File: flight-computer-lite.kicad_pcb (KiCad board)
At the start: 2 copper layers, 65 x 65 mm, 19 parts, among them J1 USB_C_Receptacle_USB2.0_16P, J2 Micro_SD_Card_Det2, Q1 BSS138, U1 RP2040, U2 W25Q32JVZP, U3 ICM-42688-P, U4 BMI088, U5 LIS3MDL, U6 MS5611-01BA, U7 SHT4x, U8 SAM-M8Q

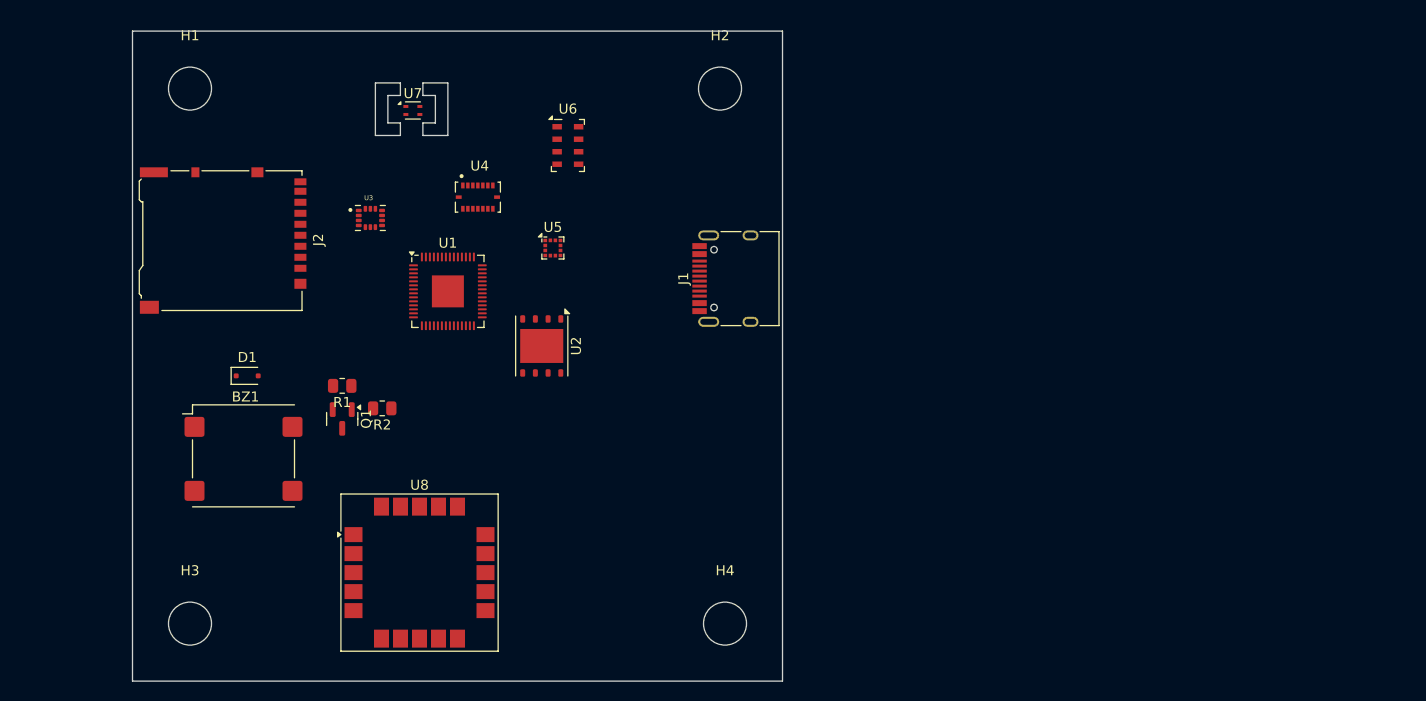
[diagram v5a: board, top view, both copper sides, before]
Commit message: Added battery, updated USB
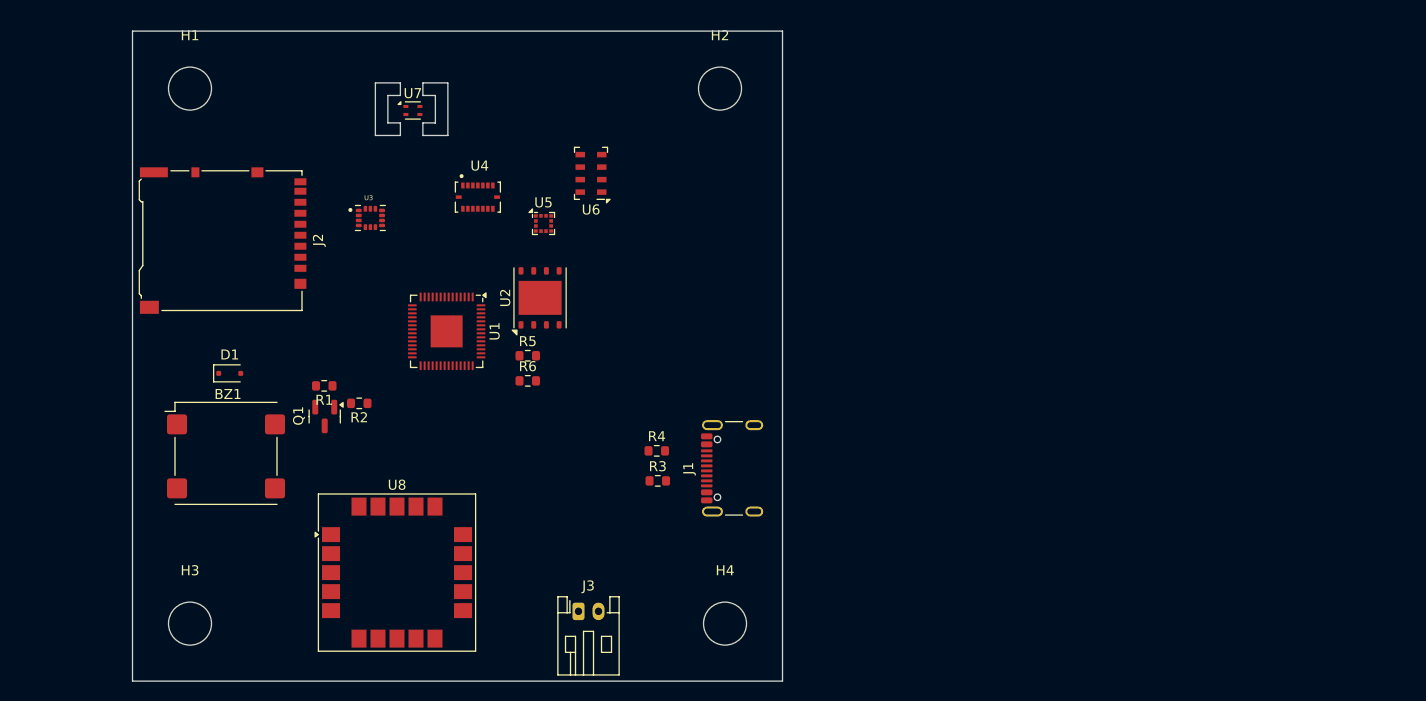
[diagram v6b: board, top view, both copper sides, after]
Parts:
- added J3: Conn_01x02_Pin, Connector_JST:JST_PH_S2B-PH-K_1x02_P2.00mm_Horizontal, F.Cu at (170.8, 113.3)
- added R3: 5.1K, Resistor_SMD:R_0603_1608Metric, F.Cu at (178.7, 100.2)
- added R4: 5.1K, Resistor_SMD:R_0603_1608Metric, F.Cu at (178.6, 97.2)
- added R5: 27.1, Resistor_SMD:R_0603_1608Metric, F.Cu at (165.7, 87.7)
- added R6: 27.1, Resistor_SMD:R_0603_1608Metric, F.Cu at (165.7, 90.2)
- J1: footprint Connector_USB:USB_C_Receptacle_HRO_TYPE-C-31-M-12 -> Connector_USB:USB_C_Receptacle_GCT_USB4105-xx-A_16P_TopMnt_Horizontal
- R1: footprint Resistor_SMD:R_0805_2012Metric -> Resistor_SMD:R_0603_1608Metric
- R2: value 100 -> 1K; footprint Resistor_SMD:R_0805_2012Metric -> Resistor_SMD:R_0603_1608Metric
- moved J1 19.0 mm to (187.2, 99.0)
- moved U2 4.82 mm to (166.9, 82.0), turned to 90 degrees
- moved U1 4.00 mm to (157.6, 85.3), turned to -90 degrees
- moved U6 3.62 mm to (172.0, 69.5), turned to 180 degrees
- moved U5 2.62 mm to (167.2, 74.5)
- moved R2 2.35 mm to (148.8, 92.5)
- moved U8 2.25 mm to (152.6, 109.4)
- moved R1 1.80 mm to (145.3, 90.8)
- moved BZ1 1.77 mm to (135.5, 97.5)
- moved D1 1.77 mm to (135.9, 89.5)
- moved Q1 1.77 mm to (145.4, 93.8)
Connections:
- net Net-(J1-VBUS-PadA4) renamed VBUS
- J1 pad A5: unconnected-(J1-CC1-PadA5) -> Net-(J1-CC1)
- J1 pad A6: unconnected-(J1-D+-PadA6) -> /CONN_USB_D+
- J1 pad A7: unconnected-(J1-D--PadA7) -> /CONN_USB_D-
- J1 pad B5: unconnected-(J1-CC2-PadB5) -> Net-(J1-CC2)
- J1 pad B6: unconnected-(J1-D+-PadB6) -> /CONN_USB_D+
- J1 pad B7: unconnected-(J1-D--PadB7) -> /CONN_USB_D-
- J1 pad S1: unconnected-(J1-SHIELD-PadS1) -> GND
- U1 pad 46: unconnected-(U1-USB_DM-Pad46) -> /CPU_USB_D-
- U1 pad 47: unconnected-(U1-USB_DP-Pad47) -> /CPU_USB_D+
- U7 pad 4: unconnected-(U7-VSS-Pad4) -> GND

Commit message: Added buttons, LEDs, TPs, and Miku
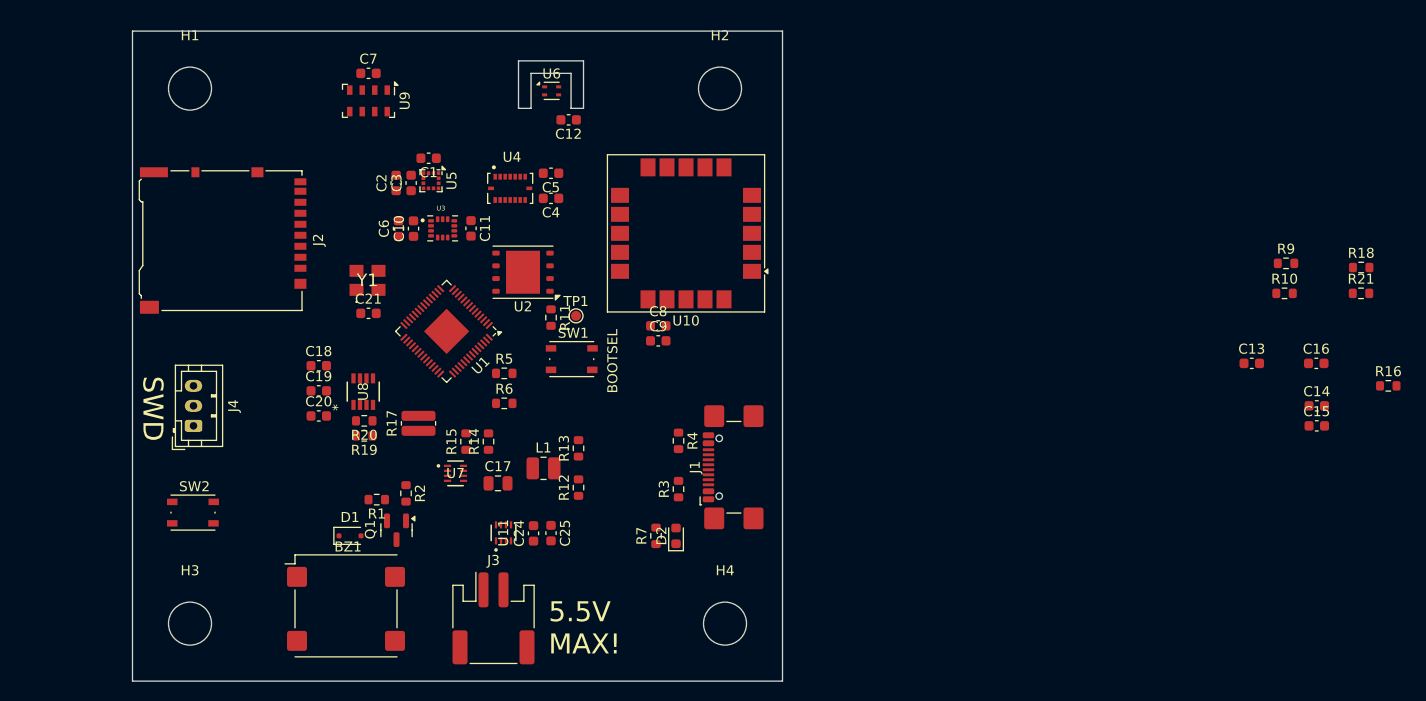
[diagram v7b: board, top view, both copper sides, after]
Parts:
- added C1: 0.1u, Capacitor_SMD:C_0603_1608Metric, F.Cu at (155.8, 68.0)
- added C10: 2.2u, Capacitor_SMD:C_0603_1608Metric, F.Cu at (154.2, 75.0)
- added C11: 10n, Capacitor_SMD:C_0603_1608Metric, F.Cu at (160.0, 75.0)
- added C12: 0.1u, Capacitor_SMD:C_0603_1608Metric, F.Cu at (169.8, 64.2)
- added C13: 0.1u, Capacitor_SMD:C_0603_1608Metric, F.Cu at (238.1, 88.5)
- added C14: 10u, Capacitor_SMD:C_0603_1608Metric, F.Cu at (244.6, 92.8)
- added C15: 0.1u, Capacitor_SMD:C_0603_1608Metric, F.Cu at (244.6, 94.8)
- added C16: 0.1u, Capacitor_SMD:C_0603_1608Metric, F.Cu at (244.5, 88.5)
- added C17: 47u, Capacitor_SMD:C_0805_2012Metric, F.Cu at (162.7, 100.5)
- added C18: 0.1u, Capacitor_SMD:C_0603_1608Metric, F.Cu at (144.8, 88.7)
- added C19: 2.2u, Capacitor_SMD:C_0603_1608Metric, F.Cu at (144.8, 91.2)
- added C2: 0.1u, Capacitor_SMD:C_0603_1608Metric, F.Cu at (152.5, 70.5)
- added C20: 0.1u, Capacitor_SMD:C_0603_1608Metric, F.Cu at (144.8, 93.8)
- added C21: 0.1u, Capacitor_SMD:C_0603_1608Metric, F.Cu at (149.8, 83.5)
- added C24: 2.2u, Capacitor_SMD:C_0603_1608Metric, F.Cu at (166.2, 105.5)
- added C25: 2.2u, Capacitor_SMD:C_0603_1608Metric, F.Cu at (168.0, 105.5)
- added C3: 1u, Capacitor_SMD:C_0603_1608Metric, F.Cu at (154.0, 70.5)
- added C4: 0.1u, Capacitor_SMD:C_0603_1608Metric, F.Cu at (168.0, 72.0)
- added C5: 0.1u, Capacitor_SMD:C_0603_1608Metric, F.Cu at (168.0, 69.5)
- added C6: 0.1u, Capacitor_SMD:C_0603_1608Metric, F.Cu at (152.8, 75.0)
- added C7: 0.1u, Capacitor_SMD:C_0603_1608Metric, F.Cu at (149.8, 59.5)
- added C8: 1u, Capacitor_SMD:C_0603_1608Metric, F.Cu at (178.7, 84.8)
- added C9: 0.1u, Capacitor_SMD:C_0603_1608Metric, F.Cu at (178.7, 86.2)
- added D2: LED, LED_SMD:LED_0603_1608Metric, F.Cu at (180.5, 105.8)
- added G***: LOGO, LRI_partlib:rocket_miku, B.Cu at (160.2, 85.2)
- added J4: Conn_01x03_Pin, Connector_JST:JST_PH_B3B-PH-K_1x03_P2.00mm_Vertical, F.Cu at (132.2, 94.8)
- added L1: 1u, Inductor_SMD:L_1008_2520Metric, F.Cu at (167.2, 99.0)
- added R10: I2C, Resistor_SMD:R_0603_1608Metric, F.Cu at (241.3, 81.5)
- added R11: 1k, Resistor_SMD:R_0603_1608Metric, F.Cu at (168.0, 83.9)
- added R12: 107k, Resistor_SMD:R_0603_1608Metric, F.Cu at (170.8, 100.9)
- added R13: 19.1k, Resistor_SMD:R_0603_1608Metric, F.Cu at (170.8, 97.0)
- added R14: 0R, Resistor_SMD:R_0603_1608Metric, F.Cu at (161.8, 96.3)
- added R15: 0R, Resistor_SMD:R_0603_1608Metric, F.Cu at (159.5, 96.3)
- added R16: 10k, Resistor_SMD:R_0603_1608Metric, F.Cu at (251.7, 90.8)
- added R17: 10m, Resistor_SMD:R_0612_1632Metric, F.Cu at (154.8, 94.5)
- added R18: I2C, Resistor_SMD:R_0603_1608Metric, F.Cu at (249.0, 78.9)
- added R19: 100, Resistor_SMD:R_0603_1608Metric, F.Cu at (149.3, 95.8)
- added R20: 100, Resistor_SMD:R_0603_1608Metric, F.Cu at (149.3, 94.2)
- added R21: I2C, Resistor_SMD:R_0603_1608Metric, F.Cu at (249.0, 81.5)
- added R7: R, Resistor_SMD:R_0603_1608Metric, F.Cu at (178.5, 105.8)
- added R9: I2C, Resistor_SMD:R_0603_1608Metric, F.Cu at (241.5, 78.5)
- added SW1: SW_Push, Button_Switch_SMD:SW_Push_1P1T_NO_Vertical_Wuerth_434133025816, F.Cu at (170.1, 88.1)
- added SW2: SW_Push, Button_Switch_SMD:SW_Push_1P1T_NO_Vertical_Wuerth_434133025816, F.Cu at (132.2, 103.4)
- added TP1: TestPoint, TestPoint:TestPoint_Pad_D1.0mm, F.Cu at (170.5, 83.8)
- added U10: SAM-M10Q, RF_GPS:ublox_SAM-M8Q, F.Cu at (181.5, 75.5)
- added U11: LM66200DRLR, LRI_partlib:LM66200, F.Cu at (163.3, 105.4)
- added U9: MS5611-01BA, Package_LGA:LGA-8_3x5mm_P1.25mm, F.Cu at (149.8, 62.2)
- added Y1: SiT1602BI-22-33E-12.000000E, LRI_partlib:SIT1602BI2233E12000000G, F.Cu at (149.7, 80.2)
- J1: footprint Connector_USB:USB_C_Receptacle_GCT_USB4105-xx-A_16P_TopMnt_Horizontal -> Connector_USB:USB_C_Receptacle_GCT_USB4110
- J3: footprint Connector_JST:JST_PH_S2B-PH-K_1x02_P2.00mm_Horizontal -> Connector_JST:JST_PH_S2B-PH-SM4-TB_1x02-1MP_P2.00mm_Horizontal
- U6: value MS5611-01BA -> SHT4x; footprint Package_LGA:LGA-8_3x5mm_P1.25mm -> Sensor_Humidity:Sensirion_DFN-4_1.5x1.5mm_P0.8mm_SHT4x_NoCentralPad
- U7: value SHT4x -> TPS631000DRLR; footprint Sensor_Humidity:Sensirion_DFN-4_1.5x1.5mm_P0.8mm_SHT4x_NoCentralPad -> LRI_partlib:TPS631000DRLR_TEX
- U8: value SAM-M8Q -> INA232AIDDFR; footprint RF_GPS:ublox_SAM-M8Q -> LRI_partlib:INA232AIDDFR
- moved U7 36.5 mm to (158.4, 99.5)
- moved D1 20.2 mm to (147.9, 105.8)
- moved BZ1 19.4 mm to (147.5, 112.8)
- moved U8 18.4 mm to (149.2, 91.3), turned to 90 degrees
- moved Q1 13.5 mm to (152.6, 105.2)
- moved R1 12.5 mm to (150.6, 102.1)
- moved U5 12.0 mm to (156.0, 70.2), turned to -90 degrees
- moved R2 10.1 mm to (153.5, 101.5), turned to -90 degrees
- moved U6 9.14 mm to (168.1, 61.2), turned to 0 degrees
- moved J3 8.53 mm to (162.2, 114.0)
- moved U3 7.30 mm to (157.2, 75.0)
- moved U4 3.34 mm to (163.9, 71.0)
- moved R6 3.25 mm to (163.3, 92.5)
- moved U2 3.08 mm to (165.2, 79.4), turned to 180 degrees
- moved R5 2.94 mm to (163.3, 89.5)
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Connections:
- net /CONN_USB_D+ renamed /USB_D+
- net /CONN_USB_D- renamed /USB_D-
- J1 pad S1: GND -> unconnected-(J1-SHIELD-PadS1)
- J2 pad 4: unconnected-(J2-VDD-Pad4) -> +3V3
- J2 pad 6: unconnected-(J2-VSS-Pad6) -> GND
- U1 pad 2: unconnected-(U1-GPIO0-Pad2) -> /I2C_1_SDA
- U1 pad 20: unconnected-(U1-XIN-Pad20) -> /XIN
- U1 pad 3: unconnected-(U1-GPIO1-Pad3) -> /I2C_1_SCL
- U1 pad 4: unconnected-(U1-GPIO2-Pad4) -> /I2C Bus 2/I2C_2_SDA
- U1 pad 5: unconnected-(U1-GPIO3-Pad5) -> /I2C Bus 2/I2C_2_SCL
- U1 pad 51: unconnected-(U1-QSPI_SD3-Pad51) -> /QSPI_SD3
- U1 pad 52: unconnected-(U1-QSPI_SCLK-Pad52) -> /QSPI_SCLK
- U1 pad 53: unconnected-(U1-QSPI_SD0-Pad53) -> /QSPI_SD0
- U1 pad 54: unconnected-(U1-QSPI_SD2-Pad54) -> /QSPI_SD2
- U1 pad 55: unconnected-(U1-QSPI_SD1-Pad55) -> /QSPI_SD1
- U1 pad 56: unconnected-(U1-QSPI_SS-Pad56) -> /QSPI_SS
- U2 pad 1: unconnected-(U2-~{CS}-Pad1) -> /QSPI_SS
- U2 pad 2: unconnected-(U2-DO(IO1)-Pad2) -> /QSPI_SD1
- U2 pad 3: unconnected-(U2-IO2-Pad3) -> /QSPI_SD2
- U2 pad 5: unconnected-(U2-DI(IO0)-Pad5) -> /QSPI_SD0
- U2 pad 6: unconnected-(U2-CLK-Pad6) -> /QSPI_SCLK
- U2 pad 7: unconnected-(U2-IO3-Pad7) -> /QSPI_SD3
- U2 pad 8: unconnected-(U2-VCC-Pad8) -> +3V3
- U3 pad 1: unconnected-(U3-AP_SDO/AP_AD0-Pad1) -> +3V3
- U3 pad 12: unconnected-(U3-AP_CS-Pad12) -> +3V3
- U3 pad 13: unconnected-(U3-AP_SCL/AP_SCLK-Pad13) -> /I2C Bus 1/I2C_1_SCL
- U3 pad 14: unconnected-(U3-AP_SDA/AP_SDIO/AP_SDI-Pad14) -> /I2C Bus 1/I2C_1_SDA
- U3 pad 5: unconnected-(U3-VDDIO-Pad5) -> +3V3
- U3 pad 8: unconnected-(U3-VDD-Pad8) -> +3V3
- U3 pad 9: unconnected-(U3-INT2/FSYNC/CLKIN-Pad9) -> GND
- U4 pad 10: unconnected-(U4-SDO2-Pad10) -> GND
- U4 pad 11: unconnected-(U4-VDDIO-Pad11) -> +3V3
- U4 pad 15: unconnected-(U4-SDO1-Pad15) -> GND
- U4 pad 3: unconnected-(U4-VDD-Pad3) -> +3V3
- U4 pad 4: unconnected-(U4-GNDA-Pad4) -> GND
- U4 pad 6: unconnected-(U4-GNDIO-Pad6) -> GND
- U4 pad 7: unconnected-(U4-PS-Pad7) -> +3V3
- U4 pad 8: unconnected-(U4-SCL/SCK-Pad8) -> /I2C Bus 2/I2C_2_SCL
- U4 pad 9: unconnected-(U4-SDA/SDI-Pad9) -> /I2C Bus 2/I2C_2_SDA
- U5 pad 1: unconnected-(U5-SCL/SPC-Pad1) -> /I2C Bus 1/I2C_1_SCL
- U5 pad 10: unconnected-(U5-~{CS}-Pad10) -> +3V3
- U5 pad 11: unconnected-(U5-SDA/SDI/SDO-Pad11) -> /I2C Bus 1/I2C_1_SDA
- U5 pad 4: unconnected-(U5-C1-Pad4) -> Net-(U5-C1)
- U5 pad 5: unconnected-(U5-Vdd-Pad5) -> +3V3
- U5 pad 6: unconnected-(U5-Vdd_IO-Pad6) -> +3V3
- U5 pad 9: unconnected-(U5-SDO/SA1-Pad9) -> GND
- U6 pad 1: unconnected-(U6-VDD-Pad1) -> /I2C Bus 1/I2C_1_SDA
- U6 pad 2: unconnected-(U6-PS-Pad2) -> /I2C Bus 1/I2C_1_SCL
- U6 pad 3: GND -> +3V3
- U6 pad 4: Net-(U6-CSB-Pad4) -> GND
- U7 pad 1: unconnected-(U7-SDA-Pad1) -> +3V3
- U7 pad 2: unconnected-(U7-SCL-Pad2) -> Net-(U7-LX2)
- U7 pad 3: unconnected-(U7-VDD-Pad3) -> Net-(U7-LX1)
- U7 pad 4: GND -> /PSU/-IN
- U8 pad 1: GND -> Net-(U8-IN+)
- U8 pad 2: unconnected-(U8-VCC_IO-Pad2) -> Net-(U8-IN-)
- U8 pad 3: unconnected-(U8-V_BCKP-Pad3) -> GND
- U8 pad 4: GND -> /PSU/+IN
- U8 pad 5: GND -> /PSU/I2C_1_SCL
- U8 pad 6: GND -> /PSU/I2C_1_SDA
- U8 pad 7: unconnected-(U8-TIMEPULSE-Pad7) -> GND
- U8 pad 8: unconnected-(U8-~{SAFEBOOT}-Pad8) -> /PSU/PMON_ALERT
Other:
- outline, holes or cut-outs redrawn
- board text added: "5.5V MAX!"
- board text added: "BOOTSEL"
- board text added: "SWD"

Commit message: Added more decoupling caps
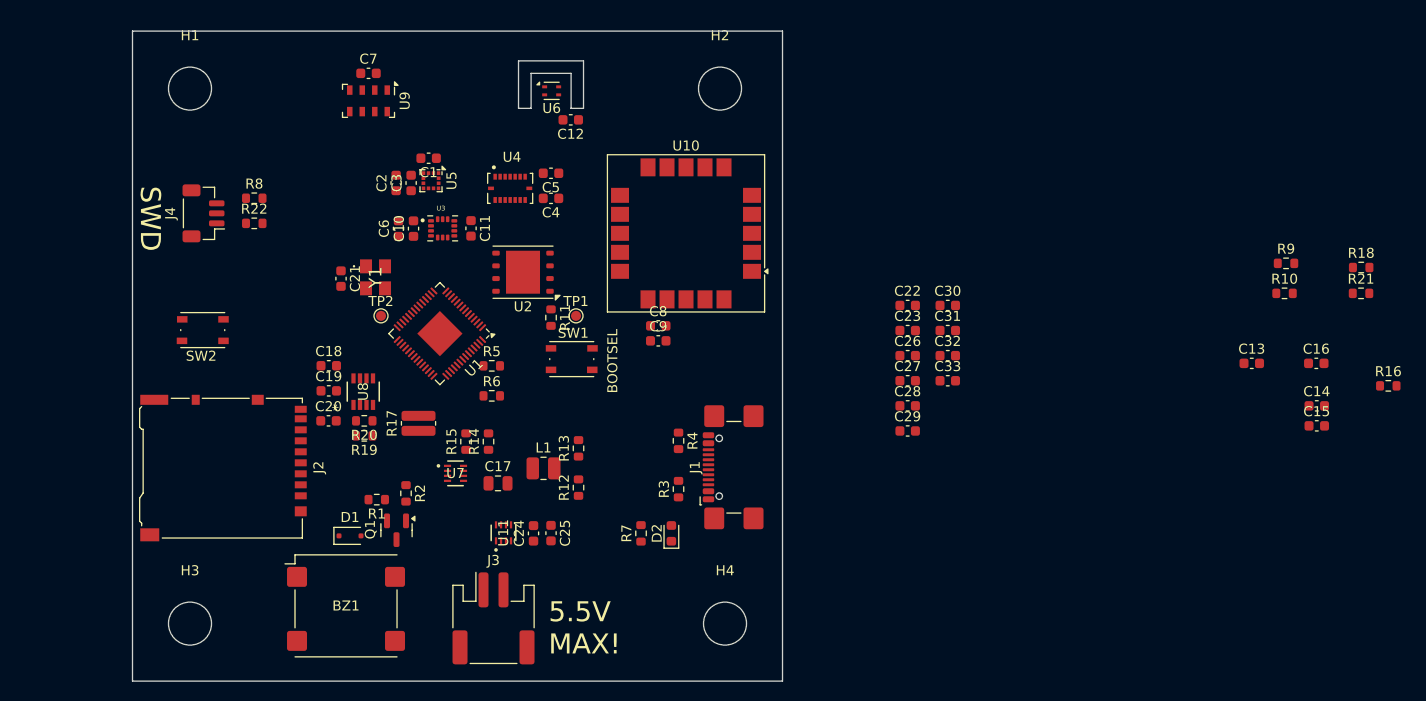
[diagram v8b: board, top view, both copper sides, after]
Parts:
- added C22: 0.1u, Capacitor_SMD:C_0603_1608Metric, F.Cu at (203.7, 82.7)
- added C23: 0.1u, Capacitor_SMD:C_0603_1608Metric, F.Cu at (203.7, 85.2)
- added C26: 0.1u, Capacitor_SMD:C_0603_1608Metric, F.Cu at (203.7, 87.7)
- added C27: 0.1u, Capacitor_SMD:C_0603_1608Metric, F.Cu at (203.7, 90.2)
- added C28: 0.1u, Capacitor_SMD:C_0603_1608Metric, F.Cu at (203.7, 92.8)
- added C29: 0.1u, Capacitor_SMD:C_0603_1608Metric, F.Cu at (203.7, 95.3)
- added C30: 2.2u, Capacitor_SMD:C_0603_1608Metric, F.Cu at (207.7, 82.7)
- added C31: 2.2u, Capacitor_SMD:C_0603_1608Metric, F.Cu at (207.7, 85.2)
- added C32: 0.1u, Capacitor_SMD:C_0603_1608Metric, F.Cu at (207.7, 87.7)
- added C33: 0.1u, Capacitor_SMD:C_0603_1608Metric, F.Cu at (207.7, 90.2)
- added R22: 100, Resistor_SMD:R_0603_1608Metric, F.Cu at (138.3, 74.5)
- added R8: 100, Resistor_SMD:R_0603_1608Metric, F.Cu at (138.3, 72.0)
- added TP2: TestPoint, TestPoint:TestPoint_Pad_D1.0mm, F.Cu at (151.0, 83.8)
- J4: footprint Connector_JST:JST_PH_B3B-PH-K_1x03_P2.00mm_Vertical -> Connector_JST:JST_SH_BM03B-SRSS-TB_1x03-1MP_P1.00mm_Vertical
- moved J2 22.8 mm to (135.2, 99.0)
- moved J4 21.3 mm to (133.2, 73.5)
- moved SW2 18.3 mm to (133.2, 85.2), turned to 180 degrees
- moved C21 4.43 mm to (147.0, 80.0), turned to -90 degrees
- moved R7 1.52 mm to (177.0, 105.5)
- moved R5 1.46 mm to (162.1, 88.8)
- moved R6 1.46 mm to (162.1, 91.8)
- moved C20 1.09 mm to (145.8, 94.2)
- moved C18 1.00 mm to (145.8, 88.7)
- moved C19 1.00 mm to (145.8, 91.2)
- moved Y1 0.85 mm to (150.4, 79.9), turned to -90 degrees
- moved U1 0.71 mm to (156.9, 85.5)
- moved D2 0.53 mm to (180.0, 105.5)
- moved C12 0.21 mm to (170.0, 64.2)
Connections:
- net Net-(U1-DVDD-Pad23) renamed +1V1
- J2 pad 10: unconnected-(J2-DET_A-Pad10) -> /SD_DET
- J2 pad 11: unconnected-(J2-SHIELD-Pad11) -> GND
- J2 pad 9: unconnected-(J2-DET_B-Pad9) -> GND
- J4 pad 1: unconnected-(J4-Pin_1-Pad1) -> /SWDIO
- J4 pad 2: unconnected-(J4-Pin_2-Pad2) -> GND
- J4 pad 3: unconnected-(J4-Pin_3-Pad3) -> /SWCLK
- SW2 pad 1: unconnected-(SW2-Pad1) -> /USR
- U1 pad 1: Net-(U1-IOVDD-Pad1) -> +3V3
- U1 pad 10: Net-(U1-IOVDD-Pad1) -> +3V3
- U1 pad 15: unconnected-(U1-GPIO12-Pad15) -> /USR
- U1 pad 19: unconnected-(U1-TESTEN-Pad19) -> GND
- U1 pad 22: Net-(U1-IOVDD-Pad1) -> +3V3
- U1 pad 24: unconnected-(U1-SWCLK-Pad24) -> /SC
- U1 pad 25: unconnected-(U1-SWD-Pad25) -> /SD
- U1 pad 26: unconnected-(U1-RUN-Pad26) -> /RUN
- U1 pad 33: Net-(U1-IOVDD-Pad1) -> +3V3
- U1 pad 38: unconnected-(U1-GPIO26_ADC0-Pad38) -> /AD0
- U1 pad 39: unconnected-(U1-GPIO27_ADC1-Pad39) -> /AD1
- U1 pad 40: unconnected-(U1-GPIO28_ADC2-Pad40) -> /AD2
- U1 pad 41: unconnected-(U1-GPIO29_ADC3-Pad41) -> /AD3
- U1 pad 42: Net-(U1-IOVDD-Pad1) -> +3V3
- U1 pad 44: unconnected-(U1-VREG_IN-Pad44) -> +3V3
- U1 pad 45: unconnected-(U1-VREG_VOUT-Pad45) -> +3V3
- U1 pad 48: unconnected-(U1-USB_VDD-Pad48) -> +3V3
- U1 pad 49: Net-(U1-IOVDD-Pad1) -> +3V3
